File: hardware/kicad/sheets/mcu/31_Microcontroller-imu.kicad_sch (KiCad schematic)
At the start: 8 parts, among them U186 LSM6DSOXTR

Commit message: reorganized
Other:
- title: Microcontroller-imu -> IMU Interface
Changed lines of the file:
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@@
 	(paper "User" 297 210)
 	(title_block
-		(title "Microcontroller-imu")
+		(title "IMU Interface")
 		(date "2026-02-16")
 	)

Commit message: before final cleanup
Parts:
- renumbered C287 to C45, C288 to C46, R558 to R89, U186 to U17, U215 to U18, U214 to U19, U213 to U20, U212 to U21
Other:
- moved on the sheet: R89

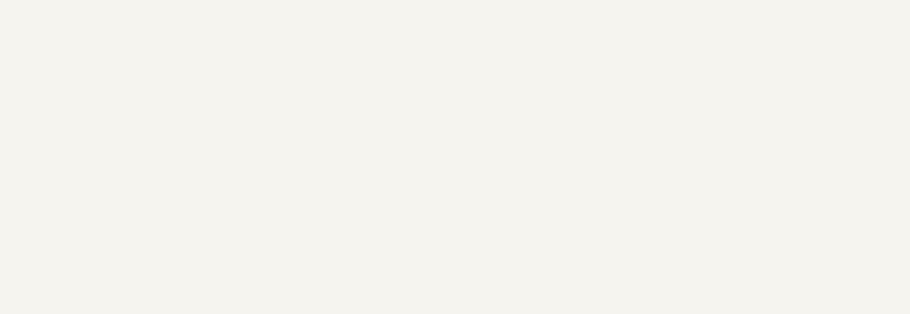
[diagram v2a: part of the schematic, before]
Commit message: better sheet nesting for power rails
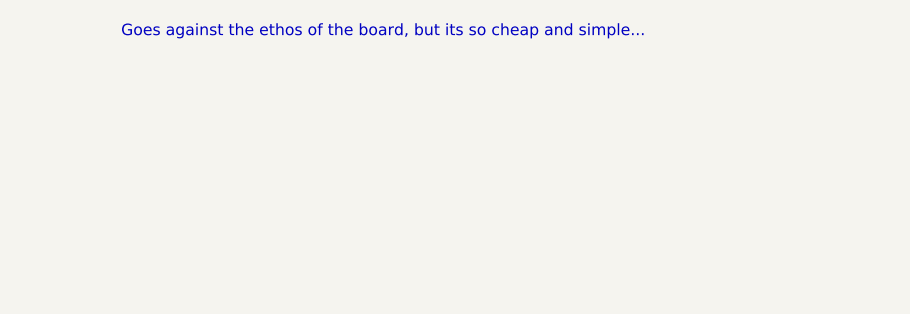
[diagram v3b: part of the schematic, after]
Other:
- note added: "Goes against the ethos of the board, but its so cheap and simple..."
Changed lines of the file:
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@@
 		(date "2026-02-16")
+	)
+	(text "Goes against the ethos of the board, but its so cheap and simple...\n"
+		(exclude_from_sim no)
+		(at 64.008 41.656 0)
+		(effects
+			(font
+				(size 1.27 1.27)
+			)
+		)
 	)
 	(text "0x6B"

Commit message: resheeted bms and fixed links for the 12v buck
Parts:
- renumbered C45 to C83, C46 to C84, R89 to R116, U17 to U32, U18 to U33, U19 to U34, U20 to U35, U21 to U36
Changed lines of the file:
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@@
 		(on_board yes)
 		(dnp no)
-		(property "Reference" "#PWR0157"
+		(property "Reference" "#PWR0109"
 			(at 97.79 81.28 0)
 			(effects
@@
 			(project "svea_powerboard_rev3"
 				(path "/3f85abf4-0b95-4c4a-b7e9-06f59ca1ea3d/5c2e021f-c2d4-49e2-8c36-9a64f1f12004/8d05c3b8-20a4-4a7f-9b20-01f8d5d5be45"
-					(reference "#PWR0157")
+					(reference "#PWR0109")
 					(unit 1)
 				)
@@
 		(on_board yes)
 		(dnp no)
-		(property "Reference" "U17"
+		(property "Reference" "U32"
 			(at 102.87 85.09 0)
 			(effects
@@
 			(project "svea_powerboard_rev3"
 				(path "/3f85abf4-0b95-4c4a-b7e9-06f59ca1ea3d/5c2e021f-c2d4-49e2-8c36-9a64f1f12004/8d05c3b8-20a4-4a7f-9b20-01f8d5d5be45"
-					(reference "U17")
+					(reference "U32")
 					(unit 1)
 				)
@@
 		(on_board yes)
 		(dnp no)
-		(property "Reference" "#PWR0160"
+		(property "Reference" "#PWR0111"
 			(at 198.12 92.71 0)
 			(effects
@@
 			(project "svea_powerboard_rev3"
 				(path "/3f85abf4-0b95-4c4a-b7e9-06f59ca1ea3d/5c2e021f-c2d4-49e2-8c36-9a64f1f12004/8d05c3b8-20a4-4a7f-9b20-01f8d5d5be45"
-					(reference "#PWR0160")
+					(reference "#PWR0111")
 					(unit 1)
 				)
@@
 		(on_board yes)
 		(dnp no)
-		(property "Reference" "R89"
+		(property "Reference" "R116"
 			(at 187.96 93.98 0)
 			(effects
@@
 			(project "svea_powerboard_rev3"
 				(path "/3f85abf4-0b95-4c4a-b7e9-06f59ca1ea3d/5c2e021f-c2d4-49e2-8c36-9a64f1f12004/8d05c3b8-20a4-4a7f-9b20-01f8d5d5be45"
-					(reference "R89")
+					(reference "R116")
 					(unit 1)
 				)
@@
 		(on_board yes)
 		(dnp no)
-		(property "Reference" "U19"
+		(property "Reference" "U34"
 			(at 144.78 83.82 0)
 			(effects
@@
 			(project "svea_powerboard_rev3"
 				(path "/3f85abf4-0b95-4c4a-b7e9-06f59ca1ea3d/5c2e021f-c2d4-49e2-8c36-9a64f1f12004/8d05c3b8-20a4-4a7f-9b20-01f8d5d5be45"
-					(reference "U19")
+					(reference "U34")
 					(unit 1)
 				)
@@
 		(on_board yes)
 		(dnp no)
-		(property "Reference" "U21"
+		(property "Reference" "U36"
 			(at 147.32 92.71 0)
 			(effects
@@
 			(project "svea_powerboard_rev3"
 				(path "/3f85abf4-0b95-4c4a-b7e9-06f59ca1ea3d/5c2e021f-c2d4-49e2-8c36-9a64f1f12004/8d05c3b8-20a4-4a7f-9b20-01f8d5d5be45"
-					(reference "U21")
+					(reference "U36")
 					(unit 1)
 				)
@@
 		(on_board yes)
 		(dnp no)
-		(property "Reference" "U20"
+		(property "Reference" "U35"
 			(at 147.32 88.9 0)
 			(effects
@@
 			(project "svea_powerboard_rev3"
 				(path "/3f85abf4-0b95-4c4a-b7e9-06f59ca1ea3d/5c2e021f-c2d4-49e2-8c36-9a64f1f12004/8d05c3b8-20a4-4a7f-9b20-01f8d5d5be45"
-					(reference "U20")
+					(reference "U35")
 					(unit 1)
 				)
@@
 		(on_board yes)
 		(dnp no)
-		(property "Reference" "C45"
+		(property "Reference" "C83"
 			(at 194.31 114.3 90)
 			(effects
@@
 			(project "svea_powerboard_rev3"
 				(path "/3f85abf4-0b95-4c4a-b7e9-06f59ca1ea3d/5c2e021f-c2d4-49e2-8c36-9a64f1f12004/8d05c3b8-20a4-4a7f-9b20-01f8d5d5be45"
-					(reference "C45")
+					(reference "C83")
 					(unit 1)
 				)
@@
 		(on_board yes)
 		(dnp no)
-		(property "Reference" "#PWR0159"
+		(property "Reference" "#PWR0112"
 			(at 198.12 127 0)
 			(effects
@@
 			(project "svea_powerboard_rev3"
 				(path "/3f85abf4-0b95-4c4a-b7e9-06f59ca1ea3d/5c2e021f-c2d4-49e2-8c36-9a64f1f12004/8d05c3b8-20a4-4a7f-9b20-01f8d5d5be45"
-					(reference "#PWR0159")
+					(reference "#PWR0112")
 					(unit 1)
 				)
@@
 		(on_board yes)
 		(dnp no)
-		(property "Reference" "U18"
+		(property "Reference" "U33"
 			(at 144.78 80.01 0)
 			(effects
@@
 			(project "svea_powerboard_rev3"
 				(path "/3f85abf4-0b95-4c4a-b7e9-06f59ca1ea3d/5c2e021f-c2d4-49e2-8c36-9a64f1f12004/8d05c3b8-20a4-4a7f-9b20-01f8d5d5be45"
-					(reference "U18")
+					(reference "U33")
 					(unit 1)
 				)
@@
 		(on_board yes)
 		(dnp no)
-		(property "Reference" "C46"
+		(property "Reference" "C84"
 			(at 209.55 114.3 90)
 			(effects
@@
 			(project "svea_powerboard_rev3"
 				(path "/3f85abf4-0b95-4c4a-b7e9-06f59ca1ea3d/5c2e021f-c2d4-49e2-8c36-9a64f1f12004/8d05c3b8-20a4-4a7f-9b20-01f8d5d5be45"
-					(reference "C46")
+					(reference "C84")
 					(unit 1)
 				)
@@
 		(on_board yes)
 		(dnp no)
-		(property "Reference" "#PWR0158"
+		(property "Reference" "#PWR0110"
 			(at 97.79 119.38 0)
 			(effects
@@
 			(project "svea_powerboard_rev3"
 				(path "/3f85abf4-0b95-4c4a-b7e9-06f59ca1ea3d/5c2e021f-c2d4-49e2-8c36-9a64f1f12004/8d05c3b8-20a4-4a7f-9b20-01f8d5d5be45"
-					(reference "#PWR0158")
-					(unit 1)
-				)
+					(reference "#PWR0110")
+					(unit 1)
+				)

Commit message: realized having 2 3v3 rails can cause issues
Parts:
- removed C83: 100nF, Capacitor_SMD:C_0603_1608Metric, symbol 5v rail sm-easyedapro:CC0603KRX7R9BB104
- removed C84: 1uF, Capacitor_SMD:C_0603_1608Metric, symbol 5v rail sm-easyedapro:CL10B105KB8NQNC
- removed R116: 10kΩ, Resistor_SMD:R_0603_1608Metric, symbol 5v rail sm-easyedapro:0603WAF1002T5E
- removed U32: LSM6DSOXTR, Package_LGA:LGA-14_3x2.5mm_P0.5mm, symbol 5v rail sm-easyedapro:LSM6DSOXTR
- removed U33, U34: ~, Jumper:SolderJumper-2_P1.3mm_Open_Pad1.0x1.5mm, symbol Jumper:Jumper_2_Open
- removed U35, U36: ~, Jumper:SolderJumper-2_P1.3mm_Bridged_Pad1.0x1.5mm, symbol Jumper:Jumper_2_Bridged
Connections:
- no-connect marks 2 -> 0
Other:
- note removed: "0x6B"
- note removed: "Goes against the ethos of the board, but its so cheap and simple..."
